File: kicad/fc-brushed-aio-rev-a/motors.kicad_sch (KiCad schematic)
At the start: 48 parts, among them J2 M1, J3 M2, J4 M3, J5 M4, J6 M5, J7 M6, J8 M7, J9 M8, Q2 2300A, Q3 2300A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

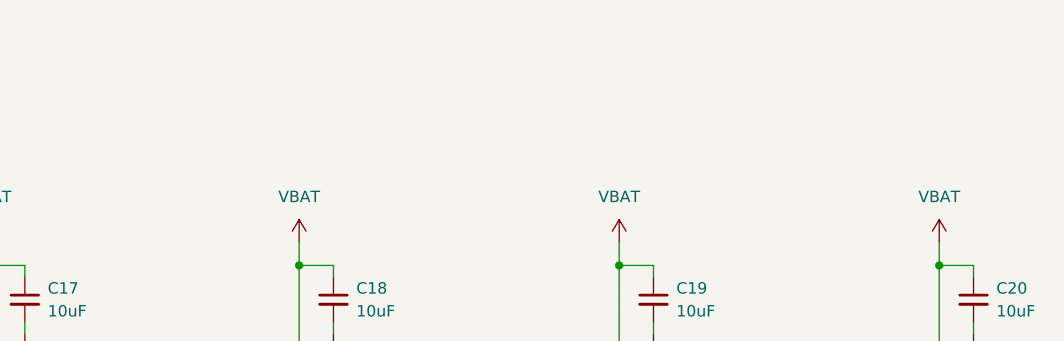
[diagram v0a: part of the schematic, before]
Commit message: Almost done with pcb! Need final checks and some silkscreen design stuff
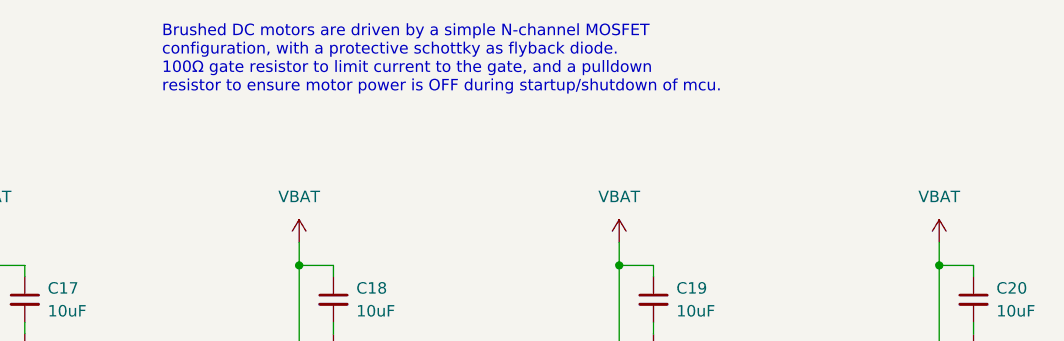
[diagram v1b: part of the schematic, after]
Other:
- note added: "Brushed DC motors are driven by a simple N-channel MOSFET configuration, with a protective schottky as flyback diode. 100Ω gate resistor to limit current to the gate, and a pulldown resistor to ensure motor power is OFF during startup/shutdown of mcu."
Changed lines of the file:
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@@
+		)
+	)
+	(text "Brushed DC motors are driven by a simple N-channel MOSFET\nconfiguration, with a protective schottky as flyback diode.\n100Ω gate resistor to limit current to the gate, and a pulldown\nresistor to ensure motor power is OFF during startup/shutdown of mcu."
+		(exclude_from_sim no)
+		(at 116.84 27.94 0)
+		(effects
+			(font
+				(size 1.27 1.27)
+			)
+			(justify left)
 		)
 	)
